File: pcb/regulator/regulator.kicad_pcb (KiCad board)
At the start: 2 copper layers, 60 x 68 mm, 0 parts

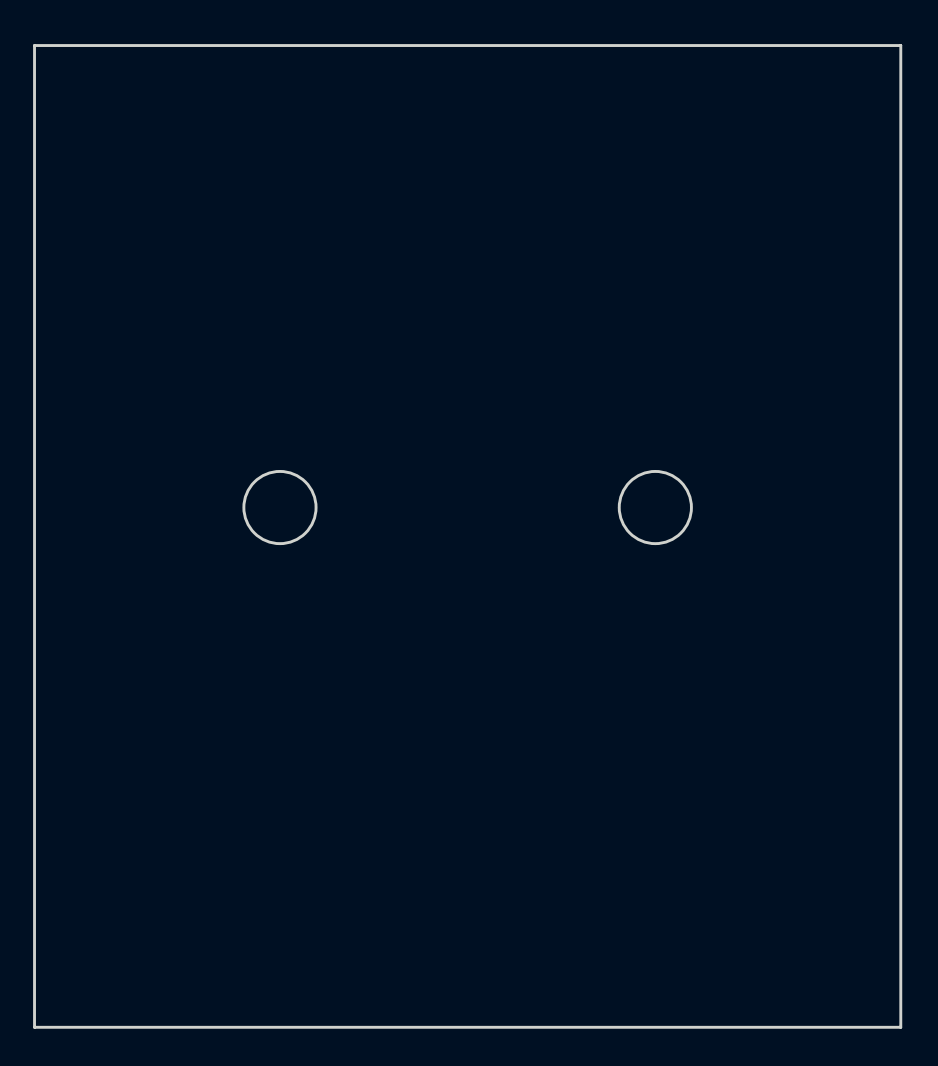
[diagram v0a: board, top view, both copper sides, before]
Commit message: PCB routing, need to polish
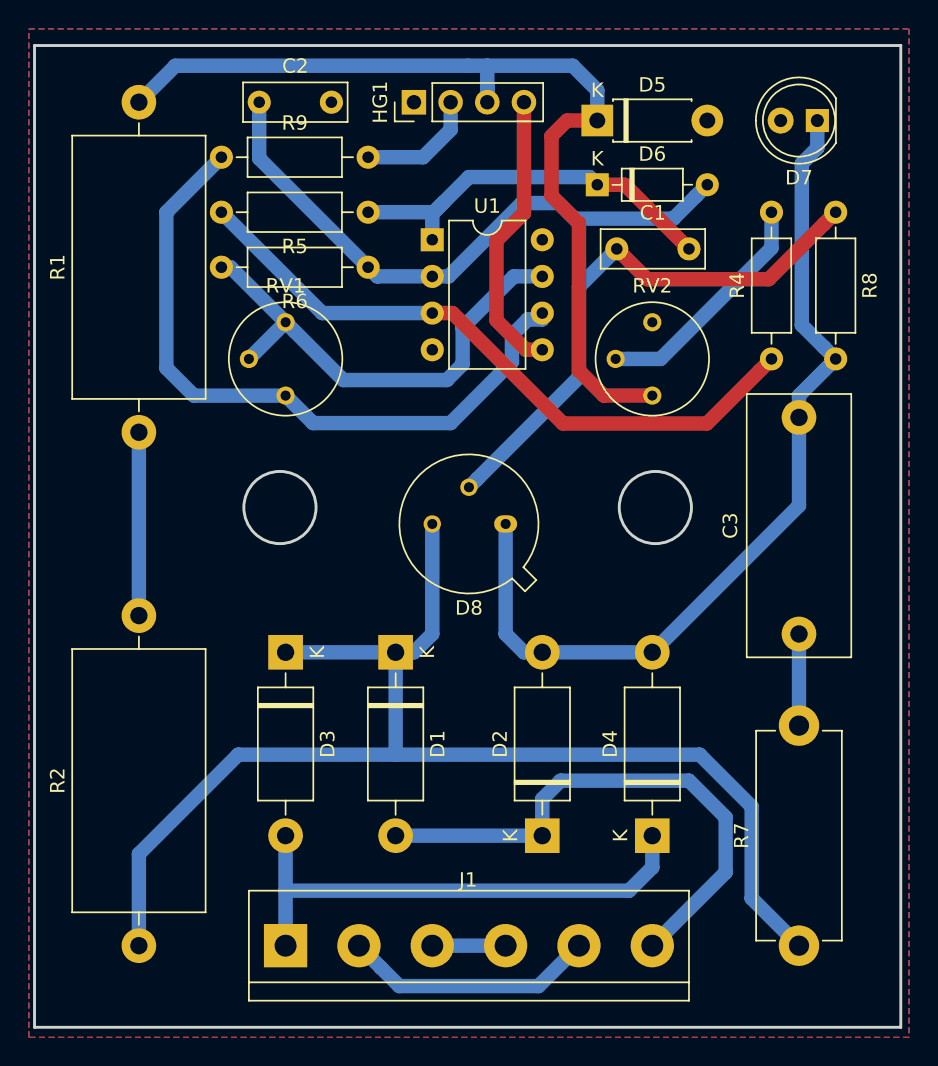
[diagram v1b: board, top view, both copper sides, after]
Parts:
- added C1: 100n, Capacitor_THT:C_Disc_D7.0mm_W2.5mm_P5.00mm, F.Cu at (158.8, 85.1)
- added C2: 33n, Capacitor_THT:C_Disc_D7.0mm_W2.5mm_P5.00mm, F.Cu at (134.1, 74.9)
- added C3: 100n/400V, Capacitor_THT:C_Rect_L18.0mm_W7.0mm_P15.00mm_FKS3_FKP3, F.Cu at (171.4, 111.8)
- added D1: D, Diode_THT:D_DO-15_P12.70mm_Horizontal, F.Cu at (143.5, 113.0)
- added D2: D, Diode_THT:D_DO-15_P12.70mm_Horizontal, F.Cu at (153.7, 125.7)
- added D3: D, Diode_THT:D_DO-15_P12.70mm_Horizontal, F.Cu at (135.9, 113.0)
- added D4: D, Diode_THT:D_DO-15_P12.70mm_Horizontal, F.Cu at (161.3, 125.7)
- added D5: 5V1, Diode_THT:D_DO-41_SOD81_P7.62mm_Horizontal, F.Cu at (157.5, 76.2)
- added D6: D, Diode_THT:D_DO-35_SOD27_P7.62mm_Horizontal, F.Cu at (157.5, 80.6)
- added D7: LED, LED_THT:LED_D5.0mm, F.Cu at (172.7, 76.2)
- added D8: Q_SCR_KGA, Package_TO_SOT_THT:TO-39-3, F.Cu at (151.1, 104.1)
- added HG1: Hall_Generator, Connector_PinHeader_2.54mm:PinHeader_1x04_P2.54mm_Vertical, F.Cu at (144.8, 74.9)
- added J1: Conn_01x06, TerminalBlock:TerminalBlock_bornier-6_P5.08mm, F.Cu at (135.9, 133.3)
- added R1: 6k8/2W, Resistor_THT:R_Axial_DIN0918_L18.0mm_D9.0mm_P22.86mm_Horizontal, F.Cu at (125.7, 97.8)
- added R2: 6k8/2W, Resistor_THT:R_Axial_DIN0918_L18.0mm_D9.0mm_P22.86mm_Horizontal, F.Cu at (125.7, 133.3)
- added R4: 820R, Resistor_THT:R_Axial_DIN0207_L6.3mm_D2.5mm_P10.16mm_Horizontal, F.Cu at (169.5, 92.7)
- added R5: 18k, Resistor_THT:R_Axial_DIN0207_L6.3mm_D2.5mm_P10.16mm_Horizontal, F.Cu at (141.6, 82.5)
- added R6: 27k, Resistor_THT:R_Axial_DIN0207_L6.3mm_D2.5mm_P10.16mm_Horizontal, F.Cu at (141.6, 86.4)
- added R7: 100R/1W, Resistor_THT:R_Axial_DIN0614_L14.3mm_D5.7mm_P15.24mm_Horizontal, F.Cu at (171.4, 133.3)
- added R8: 220R, Resistor_THT:R_Axial_DIN0207_L6.3mm_D2.5mm_P10.16mm_Horizontal, F.Cu at (174.0, 82.5)
- added R9: 100k, Resistor_THT:R_Axial_DIN0207_L6.3mm_D2.5mm_P10.16mm_Horizontal, F.Cu at (131.4, 78.7)
- added RV1: 330k, Potentiometer_THT:Potentiometer_Bourns_3339P_Vertical, F.Cu at (135.9, 95.2)
- added RV2: 15k, Potentiometer_THT:Potentiometer_Bourns_3339P_Vertical, F.Cu at (161.3, 95.2)
- added U1: TL082, Package_DIP:DIP-8_W7.62mm, F.Cu at (146.1, 84.5)
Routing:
- net Net-(D1-Pad1): track 0.00 -> 89.5 mm
- net VCC: track 0.00 -> 65.8 mm
- net Net-(C3-Pad2): track 0.00 -> 61.8 mm
- net Net-(R9-Pad1): track 0.00 -> 48.3 mm
- net Net-(R4-Pad1): track 0.00 -> 46.0 mm
- net Net-(C2-Pad1): track 0.00 -> 41.8 mm
- net Net-(C1-Pad1): track 0.00 -> 38.7 mm
- net Net-(D1-Pad2): track 0.00 -> 38.0 mm
- net Net-(D3-Pad2): track 0.00 -> 35.9 mm
- net Net-(R6-Pad2): track 0.00 -> 33.5 mm
- net Net-(C1-Pad2): track 0.00 -> 28.1 mm
- net Net-(HG1-Pad4): track 0.00 -> 19.9 mm
- net Net-(J1-Pad2): track 0.00 -> 17.6 mm
- net Net-(R4-Pad2): track 0.00 -> 16.5 mm
- net Net-(R1-Pad1): track 0.00 -> 12.7 mm
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- added copper zone on B.Cu, net GND
- added copper zone on F.Cu, net GND
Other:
- net class Default: clearance 0.2 -> 0.8; trace_width 0.25 -> 1
- rule trace_clearance: 0.2 -> 0.8
